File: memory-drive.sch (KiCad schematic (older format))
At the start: 15 parts, among them IC101 74LS157, IC11 74LS245, IC25 74LS02, IC36 74S280, IC37 74LS157, IC38 74LS157, IC52 74LS04, IC54 74LS74, IC83 74LS32, IC85 74LS04, IC88 74LS08

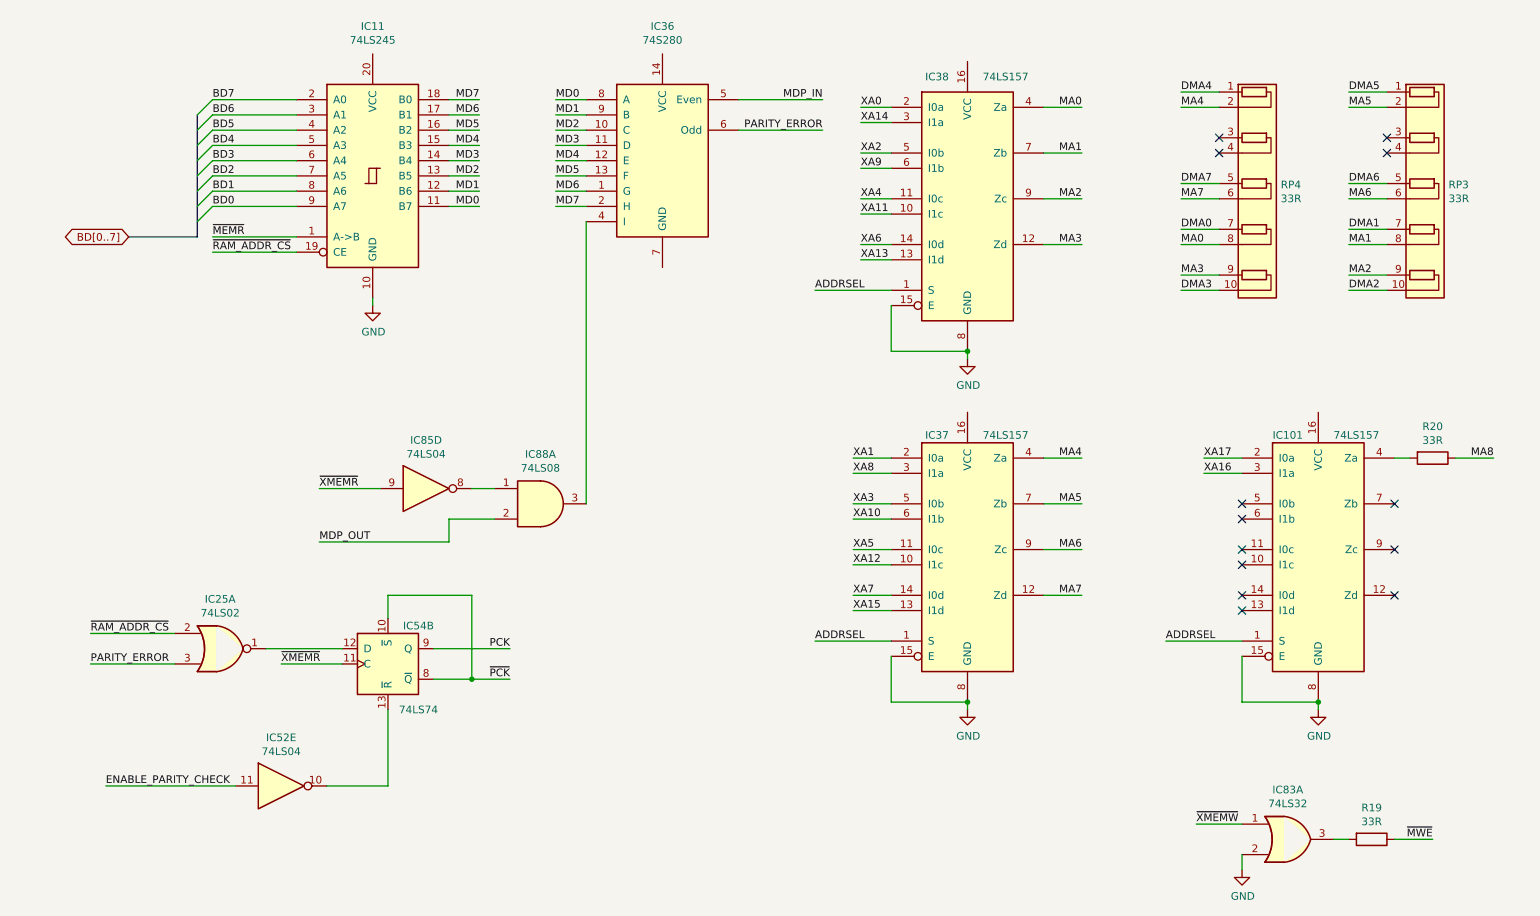
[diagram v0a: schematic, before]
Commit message: Tidy up and map all signals
This fixes up the schematic to:
 - Look presentable
 - Fix all labels connecting sheets
 - Tidy up all loose ends by either inspecting the PCB under
    magnification, measuring with an oscillosope or buzzing
    out with a meter
 - Pass ERC (with 1 exception due to incorrect circuitry around
    pin 33 on the FPU (~RQ~/~GT1~)
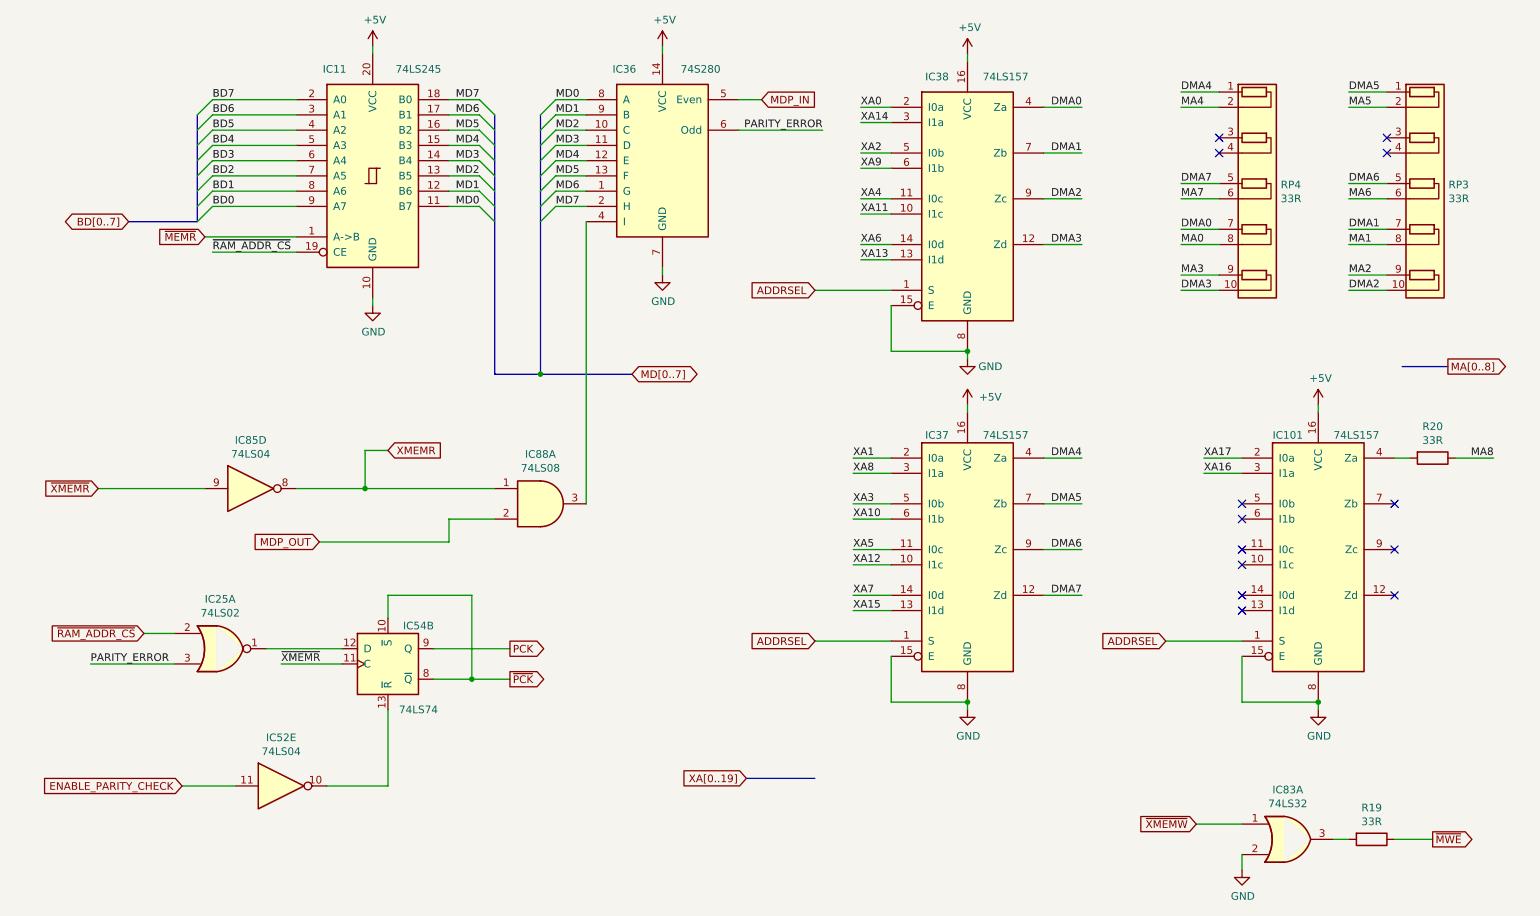
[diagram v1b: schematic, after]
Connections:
- net DMA0: now also IC38.4 (Za)
- net DMA1: now also IC38.7 (Zb)
- net DMA2: now also IC38.9 (Zc)
- net DMA3: now also IC38.12 (Zd)
- net DMA4: now also IC37.4 (Za)
- net DMA5: now also IC37.7 (Zb)
- net DMA6: now also IC37.9 (Zc)
- net DMA7: now also IC37.12 (Zd)
- net GND: now also IC36.7 (GND)
- net MA0: no longer IC38.4 (Za)
- net MA1: no longer IC38.7 (Zb)
- net MA2: no longer IC38.9 (Zc)
- net MA3: no longer IC38.12 (Zd)
- net MA4: no longer IC37.4 (Za)
- net MA5: no longer IC37.7 (Zb)
- net MA6: no longer IC37.9 (Zc)
- net MA7: no longer IC37.12 (Zd)
- net +5V: now reaches IC11.20 (VCC)
- net +5V: now also IC101.16 (VCC), IC36.14 (VCC), IC37.16 (VCC), IC38.16 (VCC)
- net XMEMR: now reaches IC85.8, IC88.1
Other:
- moved on the sheet: IC85D
